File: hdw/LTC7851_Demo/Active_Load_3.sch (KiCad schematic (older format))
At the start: 0 parts

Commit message: Added active load sheets
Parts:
- added J? (x2): ISNS, symbol Connector_Generic:Conn_01x02
- added Q? (x2): BSC123N10LSGATMA1, Package_TO_SOT_SMD:TDSON-8-1, symbol Transistor_FET:BSC123N10LSG
- added R? (x2): 5m, symbol Custom_Library:R_Custom
- added R? (x2): 10k, symbol Custom_Library:R_Custom
- added R? (x2): 10, symbol Custom_Library:R_Custom
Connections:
- net labels added: +5V, GND, LOAD_GATE
- wire segments 0 -> 12

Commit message: Annotated schematic
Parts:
- gave numbers to parts that had none: 10
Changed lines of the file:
@@
 $EndDescr
 $Comp
-L Transistor_FET:BSC123N10LSG Q?
+L Transistor_FET:BSC123N10LSG Q1301
 U 1 1 5BC437D6
 P 7900 2420
-F 0 "Q?" H 8100 2495 50  0000 L CNN
+F 0 "Q1301" H 8100 2495 50  0000 L CNN
 F 1 "BSC123N10LSGATMA1" H 8100 2420 50  0000 L CNN
 F 2 "Package_TO_SOT_SMD:TDSON-8-1" H 8100 2345 50  0001 L CIN
@@
 	8000 2790 8000 2700
 $Comp
-L power:GND #PWR?
+L power:GND #PWR01304
 U 1 1 5BC437DE
 P 8000 3090
-F 0 "#PWR?" H 8000 2840 50  0001 C CNN
+F 0 "#PWR01304" H 8000 2840 50  0001 C CNN
 F 1 "GND" H 8000 2940 50  0000 C CNN
 F 2 "" H 8000 3090 50  0001 C CNN
@@
 $EndComp
 $Comp
-L Connector_Generic:Conn_01x02 J?
+L Connector_Generic:Conn_01x02 J1301
 U 1 1 5BC437E4
 P 8830 2700
-F 0 "J?" H 8830 2800 50  0000 C CNN
+F 0 "J1301" H 8830 2800 50  0000 C CNN
 F 1 "ISNS" H 8830 2500 50  0000 C CNN
 F 2 "" H 8830 2700 50  0001 C CNN
@@
 	8000 2700 8000 2620
 $Comp
-L power:GND #PWR?
+L power:GND #PWR01307
 U 1 1 5BC437EE
 P 8630 2800
-F 0 "#PWR?" H 8630 2550 50  0001 C CNN
+F 0 "#PWR01307" H 8630 2550 50  0001 C CNN
 F 1 "GND" H 8630 2650 50  0000 C CNN
 F 2 "" H 8630 2800 50  0001 C CNN
@@
 AR Path="/5BB86F29/5BC437F8" Ref="R?"  Part="1"
 AR Path="/5BBF20D5/5BC437F8" Ref="R?"  Part="1"
-F 0 "R?" H 7900 2940 50  0000 R CNN
+AR Path="/5BBF20DB/5BC437F8" Ref="R1305"  Part="1"
+F 0 "R1305" H 7900 2940 50  0000 R CNN
 F 1 "5m" V 8000 2940 50  0000 C CNN
 F 2 "" H 8000 2940 50  0001 C CNN
@@
 $EndComp
 $Comp
-L power:+5V #PWR?
+L power:+5V #PWR01303
 U 1 1 5BC437FF
 P 8000 2220
-F 0 "#PWR?" H 8000 2070 50  0001 C CNN
+F 0 "#PWR01303" H 8000 2070 50  0001 C CNN
 F 1 "+5V" H 8000 2360 50  0000 C CNN
 F 2 "" H 8000 2220 50  0001 C CNN
@@
 AR Path="/5BB86F23/5BC43809" Ref="R?"  Part="1"
 AR Path="/5BBF20D5/5BC43809" Ref="R?"  Part="1"
-F 0 "R?" H 7140 2640 50  0000 R CNN
+AR Path="/5BBF20DB/5BC43809" Ref="R1303"  Part="1"
+F 0 "R1303" H 7140 2640 50  0000 R CNN
 F 1 "10k" V 7240 2640 50  0000 C CNN
 F 2 "" H 7240 2640 50  0001 C CNN
@@
 $EndComp
 $Comp
-L power:GND #PWR?
+L power:GND #PWR01301
 U 1 1 5BC43810
 P 7240 2790
-F 0 "#PWR?" H 7240 2540 50  0001 C CNN
+F 0 "#PWR01301" H 7240 2540 50  0001 C CNN
 F 1 "GND" H 7240 2640 50  0000 C CNN
 F 2 "" H 7240 2790 50  0001 C CNN
@@
 	7240 2420 7700 2420
 $Comp
-L Custom_Library:R_Custom R?
+L Custom_Library:R_Custom R1301
 U 1 1 5BC4381C
 P 6560 2420
-F 0 "R?" V 6460 2420 50  0000 C CNN
+F 0 "R1301" V 6460 2420 50  0000 C CNN
 F 1 "10" V 6560 2420 50  0000 C CNN
 F 2 "" H 6560 2420 50  0001 C CNN
@@
 LOAD_GATE
 $Comp
-L Transistor_FET:BSC123N10LSG Q?
+L Transistor_FET:BSC123N10LSG Q1302
 U 1 1 5BC43827
 P 7900 4460
-F 0 "Q?" H 8100 4535 50  0000 L CNN
+F 0 "Q1302" H 8100 4535 50  0000 L CNN
 F 1 "BSC123N10LSGATMA1" H 8100 4460 50  0000 L CNN
 F 2 "Package_TO_SOT_SMD:TDSON-8-1" H 8100 4385 50  0001 L CIN
@@
 	8000 4830 8000 4740
 $Comp
-L power:GND #PWR?
+L power:GND #PWR01306
 U 1 1 5BC4382F
 P 8000 5130
-F 0 "#PWR?" H 8000 4880 50  0001 C CNN
+F 0 "#PWR01306" H 8000 4880 50  0001 C CNN
 F 1 "GND" H 8000 4980 50  0000 C CNN
 F 2 "" H 8000 5130 50  0001 C CNN
@@
 $EndComp
 $Comp
-L Connector_Generic:Conn_01x02 J?
+L Connector_Generic:Conn_01x02 J1302
 U 1 1 5BC43835
 P 8830 4740
-F 0 "J?" H 8830 4840 50  0000 C CNN
+F 0 "J1302" H 8830 4840 50  0000 C CNN
 F 1 "ISNS" H 8830 4540 50  0000 C CNN
 F 2 "" H 8830 4740 50  0001 C CNN
@@
 	8000 4740 8000 4660
 $Comp
-L power:GND #PWR?
+L power:GND #PWR01308
 U 1 1 5BC4383F
 P 8630 4840
-F 0 "#PWR?" H 8630 4590 50  0001 C CNN
+F 0 "#PWR01308" H 8630 4590 50  0001 C CNN
 F 1 "GND" H 8630 4690 50  0000 C CNN
 F 2 "" H 8630 4840 50  0001 C CNN
@@
 AR Path="/5BB86F29/5BC43849" Ref="R?"  Part="1"
 AR Path="/5BBF20D5/5BC43849" Ref="R?"  Part="1"
-F 0 "R?" H 7900 4980 50  0000 R CNN
+AR Path="/5BBF20DB/5BC43849" Ref="R1306"  Part="1"
+F 0 "R1306" H 7900 4980 50  0000 R CNN
 F 1 "5m" V 8000 4980 50  0000 C CNN
 F 2 "" H 8000 4980 50  0001 C CNN
@@
 $EndComp
 $Comp
-L power:+5V #PWR?
+L power:+5V #PWR01305
 U 1 1 5BC43850
 P 8000 4260
-F 0 "#PWR?" H 8000 4110 50  0001 C CNN
+F 0 "#PWR01305" H 8000 4110 50  0001 C CNN
 F 1 "+5V" H 8000 4400 50  0000 C CNN
 F 2 "" H 8000 4260 50  0001 C CNN
@@
 AR Path="/5BB86F23/5BC4385A" Ref="R?"  Part="1"
 AR Path="/5BBF20D5/5BC4385A" Ref="R?"  Part="1"
-F 0 "R?" H 7140 4680 50  0000 R CNN
+AR Path="/5BBF20DB/5BC4385A" Ref="R1304"  Part="1"
+F 0 "R1304" H 7140 4680 50  0000 R CNN
 F 1 "10k" V 7240 4680 50  0000 C CNN
 F 2 "" H 7240 4680 50  0001 C CNN
@@
 $EndComp
 $Comp
-L power:GND #PWR?
+L power:GND #PWR01302
 U 1 1 5BC43861
 P 7240 4830
-F 0 "#PWR?" H 7240 4580 50  0001 C CNN
+F 0 "#PWR01302" H 7240 4580 50  0001 C CNN
 F 1 "GND" H 7240 4680 50  0000 C CNN
 F 2 "" H 7240 4830 50  0001 C CNN
@@
 	7240 4460 7700 4460
 $Comp
-L Custom_Library:R_Custom R?
+L Custom_Library:R_Custom R1302
 U 1 1 5BC4386D
 P 6560 4460
-F 0 "R?" V 6460 4460 50  0000 C CNN
+F 0 "R1302" V 6460 4460 50  0000 C CNN
 F 1 "10" V 6560 4460 50  0000 C CNN
 F 2 "" H 6560 4460 50  0001 C CNN

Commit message: Added Digi-Key part numbers for all parts
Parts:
- R1301, R1302: Digi-Key PN PN -> YAG3351CT-ND
- R1303, R1304: Digi-Key PN PN -> RHM10KADCT-ND
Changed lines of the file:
@@
 F 5 "1%" H 7320 2640 50  0000 L CNN "Tolerance"
 F 6 "1/10W" H 7320 2560 50  0000 L CNN "Wattage"
-F 7 "PN" H 7540 3040 60  0001 C CNN "Digi-Key PN"
+F 7 "RHM10KADCT-ND" H 7540 3040 60  0001 C CNN "Digi-Key PN"
 	1    7240 2640
 	1    0    0    -1
@@
 F 5 "1%" V 6760 2420 50  0000 C CNN "Tolerance"
 F 6 "1/10W" V 6860 2420 50  0000 C CNN "Wattage"
-F 7 "PN" H 6860 2820 60  0001 C CNN "Digi-Key PN"
+F 7 "YAG3351CT-ND" H 6860 2820 60  0001 C CNN "Digi-Key PN"
 	1    6560 2420
 	0    1    1    0
@@
 F 5 "1%" H 7320 4680 50  0000 L CNN "Tolerance"
 F 6 "1/10W" H 7320 4600 50  0000 L CNN "Wattage"
-F 7 "PN" H 7540 5080 60  0001 C CNN "Digi-Key PN"
+F 7 "RHM10KADCT-ND" H 7540 5080 60  0001 C CNN "Digi-Key PN"
 	1    7240 4680
 	1    0    0    -1
@@
 F 5 "1%" V 6760 4460 50  0000 C CNN "Tolerance"
 F 6 "1/10W" V 6860 4460 50  0000 C CNN "Wattage"
-F 7 "PN" H 6860 4860 60  0001 C CNN "Digi-Key PN"
+F 7 "YAG3351CT-ND" H 6860 4860 60  0001 C CNN "Digi-Key PN"
 	1    6560 4460
 	0    1    1    0

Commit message: Assigned footprints
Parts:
- J1301, J1302: footprint (none) -> Pin_Headers:Pin_Header_Straight_1x02_Pitch2.54mm
- Q1301, Q1302: footprint Package_TO_SOT_SMD:TDSON-8-1 -> TO_SOT_Packages_SMD:TDSON-8-1
- R1301, R1302, R1303, R1304: footprint (none) -> Resistors_SMD:R_0603
- R1305, R1306: footprint (none) -> Resistors_SMD:R_2512
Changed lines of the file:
@@
 F 0 "Q1301" H 8100 2495 50  0000 L CNN
 F 1 "BSC123N10LSGATMA1" H 8100 2420 50  0000 L CNN
-F 2 "Package_TO_SOT_SMD:TDSON-8-1" H 8100 2345 50  0001 L CIN
+F 2 "TO_SOT_Packages_SMD:TDSON-8-1" H 8100 2345 50  0001 L CIN
 F 3 "http://www.infineon.com/dgdl/Infineon-BSC123N10LS-DS-v02_08-en.pdf?fileId=db3a30431b3e89eb011b4626974b7df5" V 7900 2420 50  0001 L CNN
 F 4 "BSC123N10LSGATMA1CT-ND" H 7900 2420 50  0001 C CNN "Digi-Key PN"
@@
 F 0 "J1301" H 8830 2800 50  0000 C CNN
 F 1 "ISNS" H 8830 2500 50  0000 C CNN
-F 2 "" H 8830 2700 50  0001 C CNN
+F 2 "Pin_Headers:Pin_Header_Straight_1x02_Pitch2.54mm" H 8830 2700 50  0001 C CNN
 F 3 "~" H 8830 2700 50  0001 C CNN
 	1    8830 2700
@@
 F 0 "R1305" H 7900 2940 50  0000 R CNN
 F 1 "5m" V 8000 2940 50  0000 C CNN
-F 2 "" H 8000 2940 50  0001 C CNN
+F 2 "Resistors_SMD:R_2512" H 8000 2940 50  0001 C CNN
 F 3 "" H 8000 2940 50  0001 C CNN
 F 4 "YAG2145CT-ND" H 8300 3340 60  0001 C CNN "Digi-Key PN"
@@
 F 0 "R1303" H 7140 2640 50  0000 R CNN
 F 1 "10k" V 7240 2640 50  0000 C CNN
-F 2 "" H 7240 2640 50  0001 C CNN
+F 2 "Resistors_SMD:R_0603" H 7240 2640 50  0001 C CNN
 F 3 "" H 7240 2640 50  0001 C CNN
 F 4 "0603" H 7320 2720 50  0000 L CNN "display_footprint"
@@
 F 0 "R1301" V 6460 2420 50  0000 C CNN
 F 1 "10" V 6560 2420 50  0000 C CNN
-F 2 "" H 6560 2420 50  0001 C CNN
+F 2 "Resistors_SMD:R_0603" H 6560 2420 50  0001 C CNN
 F 3 "" H 6560 2420 50  0001 C CNN
 F 4 "0603" V 6660 2420 50  0000 C CNN "display_footprint"
@@
 F 0 "Q1302" H 8100 4535 50  0000 L CNN
 F 1 "BSC123N10LSGATMA1" H 8100 4460 50  0000 L CNN
-F 2 "Package_TO_SOT_SMD:TDSON-8-1" H 8100 4385 50  0001 L CIN
+F 2 "TO_SOT_Packages_SMD:TDSON-8-1" H 8100 4385 50  0001 L CIN
 F 3 "http://www.infineon.com/dgdl/Infineon-BSC123N10LS-DS-v02_08-en.pdf?fileId=db3a30431b3e89eb011b4626974b7df5" V 7900 4460 50  0001 L CNN
 F 4 "BSC123N10LSGATMA1CT-ND" H 7900 4460 50  0001 C CNN "Digi-Key PN"
@@
 F 0 "J1302" H 8830 4840 50  0000 C CNN
 F 1 "ISNS" H 8830 4540 50  0000 C CNN
-F 2 "" H 8830 4740 50  0001 C CNN
+F 2 "Pin_Headers:Pin_Header_Straight_1x02_Pitch2.54mm" H 8830 4740 50  0001 C CNN
 F 3 "~" H 8830 4740 50  0001 C CNN
 	1    8830 4740
@@
 F 0 "R1306" H 7900 4980 50  0000 R CNN
 F 1 "5m" V 8000 4980 50  0000 C CNN
-F 2 "" H 8000 4980 50  0001 C CNN
+F 2 "Resistors_SMD:R_2512" H 8000 4980 50  0001 C CNN
 F 3 "" H 8000 4980 50  0001 C CNN
 F 4 "YAG2145CT-ND" H 8300 5380 60  0001 C CNN "Digi-Key PN"
@@
 F 0 "R1304" H 7140 4680 50  0000 R CNN
 F 1 "10k" V 7240 4680 50  0000 C CNN
-F 2 "" H 7240 4680 50  0001 C CNN
+F 2 "Resistors_SMD:R_0603" H 7240 4680 50  0001 C CNN
 F 3 "" H 7240 4680 50  0001 C CNN
 F 4 "0603" H 7320 4760 50  0000 L CNN "display_footprint"
@@
 F 0 "R1302" V 6460 4460 50  0000 C CNN
 F 1 "10" V 6560 4460 50  0000 C CNN
-F 2 "" H 6560 4460 50  0001 C CNN
+F 2 "Resistors_SMD:R_0603" H 6560 4460 50  0001 C CNN
 F 3 "" H 6560 4460 50  0001 C CNN
 F 4 "0603" V 6660 4460 50  0000 C CNN "display_footprint"

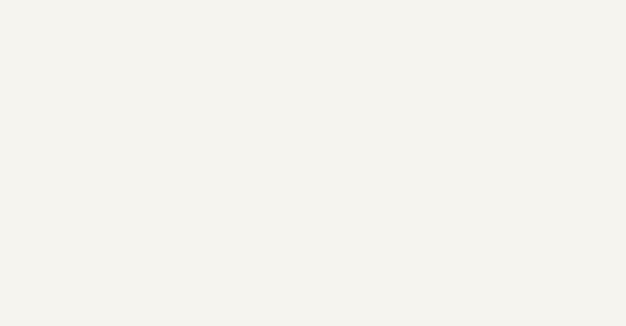
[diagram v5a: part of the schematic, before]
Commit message: Added page titles
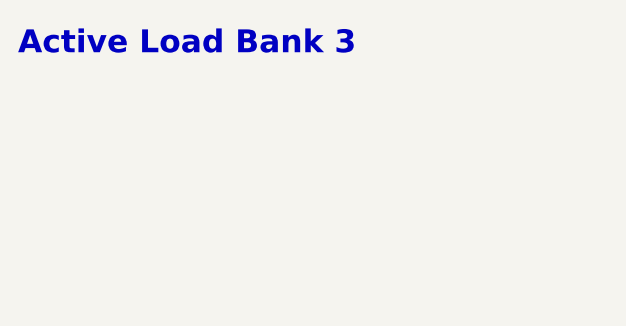
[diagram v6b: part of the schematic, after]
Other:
- note added: "Active Load Bank 3"
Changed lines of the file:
@@
 Text GLabel 6410 4460 0    50   Input ~ 0
 LOAD_GATE
+Text Notes 540  690  0    100  ~ 20
+Active Load Bank 3
 $EndSCHEMATC

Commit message: Placed phases on board
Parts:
- removed J1301, J1302: ISNS, Pin_Headers:Pin_Header_Straight_1x02_Pitch2.54mm, symbol Connector_Generic:Conn_01x02
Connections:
- wire segments 12 -> 8
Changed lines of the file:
@@
 	1    0    0    -1
 $EndComp
-Wire Wire Line
-	8000 2790 8000 2700
 $Comp
 L power:GND #PWR01304
@@
 F 3 "" H 8000 3090 50  0001 C CNN
 	1    8000 3090
-	1    0    0    -1
-$EndComp
-$Comp
-L Connector_Generic:Conn_01x02 J1301
-U 1 1 5BC437E4
-P 8830 2700
-F 0 "J1301" H 8830 2800 50  0000 C CNN
-F 1 "ISNS" H 8830 2500 50  0000 C CNN
-F 2 "Pin_Headers:Pin_Header_Straight_1x02_Pitch2.54mm" H 8830 2700 50  0001 C CNN
-F 3 "~" H 8830 2700 50  0001 C CNN
-	1    8830 2700
-	1    0    0    -1
-$EndComp
-Wire Wire Line
-	8630 2700 8000 2700
-Connection ~ 8000 2700
-Wire Wire Line
-	8000 2700 8000 2620
-$Comp
-L power:GND #PWR01307
-U 1 1 5BC437EE
-P 8630 2800
-F 0 "#PWR01307" H 8630 2550 50  0001 C CNN
-F 1 "GND" H 8630 2650 50  0000 C CNN
-F 2 "" H 8630 2800 50  0001 C CNN
-F 3 "" H 8630 2800 50  0001 C CNN
-	1    8630 2800
 	1    0    0    -1
 $EndComp
@@
 	1    0    0    -1
 $EndComp
-Wire Wire Line
-	8000 4830 8000 4740
 $Comp
 L power:GND #PWR01306
@@
 F 3 "" H 8000 5130 50  0001 C CNN
 	1    8000 5130
-	1    0    0    -1
-$EndComp
-$Comp
-L Connector_Generic:Conn_01x02 J1302
-U 1 1 5BC43835
-P 8830 4740
-F 0 "J1302" H 8830 4840 50  0000 C CNN
-F 1 "ISNS" H 8830 4540 50  0000 C CNN
-F 2 "Pin_Headers:Pin_Header_Straight_1x02_Pitch2.54mm" H 8830 4740 50  0001 C CNN
-F 3 "~" H 8830 4740 50  0001 C CNN
-	1    8830 4740
-	1    0    0    -1
-$EndComp
-Wire Wire Line
-	8630 4740 8000 4740
-Connection ~ 8000 4740
-Wire Wire Line
-	8000 4740 8000 4660
-$Comp
-L power:GND #PWR01308
-U 1 1 5BC4383F
-P 8630 4840
-F 0 "#PWR01308" H 8630 4590 50  0001 C CNN
-F 1 "GND" H 8630 4690 50  0000 C CNN
-F 2 "" H 8630 4840 50  0001 C CNN
-F 3 "" H 8630 4840 50  0001 C CNN
-	1    8630 4840
 	1    0    0    -1
 $EndComp
@@
 Text Notes 540  690  0    100  ~ 20
 Active Load Bank 3
+Wire Wire Line
+	8000 2620 8000 2790
+Wire Wire Line
+	8000 4660 8000 4830
 $EndSCHEMATC

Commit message: Added a few connectors and cleaned up some routing
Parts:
- Q1301, Q1302: value BSC123N10LSGATMA1 -> IPC100N04S51R7ATMA1
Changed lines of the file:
@@
 P 7900 2420
 F 0 "Q1301" H 8100 2495 50  0000 L CNN
-F 1 "BSC123N10LSGATMA1" H 8100 2420 50  0000 L CNN
+F 1 "IPC100N04S51R7ATMA1" H 8100 2420 50  0000 L CNN
 F 2 "TO_SOT_Packages_SMD:TDSON-8-1" H 8100 2345 50  0001 L CIN
 F 3 "http://www.infineon.com/dgdl/Infineon-BSC123N10LS-DS-v02_08-en.pdf?fileId=db3a30431b3e89eb011b4626974b7df5" V 7900 2420 50  0001 L CNN
@@
 P 7900 4460
 F 0 "Q1302" H 8100 4535 50  0000 L CNN
-F 1 "BSC123N10LSGATMA1" H 8100 4460 50  0000 L CNN
+F 1 "IPC100N04S51R7ATMA1" H 8100 4460 50  0000 L CNN
 F 2 "TO_SOT_Packages_SMD:TDSON-8-1" H 8100 4385 50  0001 L CIN
 F 3 "http://www.infineon.com/dgdl/Infineon-BSC123N10LS-DS-v02_08-en.pdf?fileId=db3a30431b3e89eb011b4626974b7df5" V 7900 4460 50  0001 L CNN
